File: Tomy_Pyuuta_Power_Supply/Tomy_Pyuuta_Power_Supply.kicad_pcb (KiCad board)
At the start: 2 copper layers, 125 x 45 mm, 15 parts, among them J1 Power In (+12VDC), J2 Power Out, J3 Power LED, U1 +5V Regulator, U2 -5V Regulator

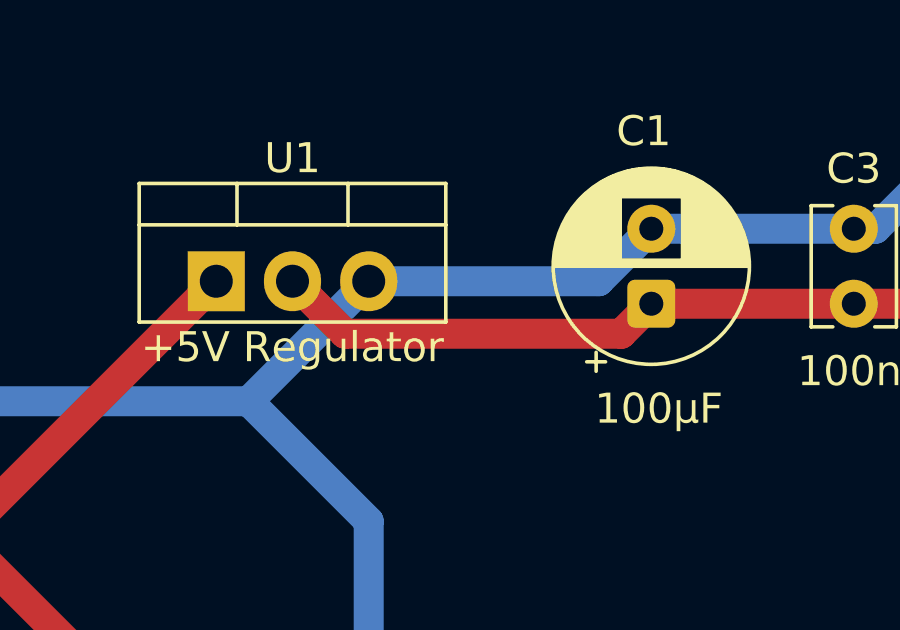
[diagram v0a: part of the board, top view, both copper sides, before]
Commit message: Fixed 5V regulator pinout
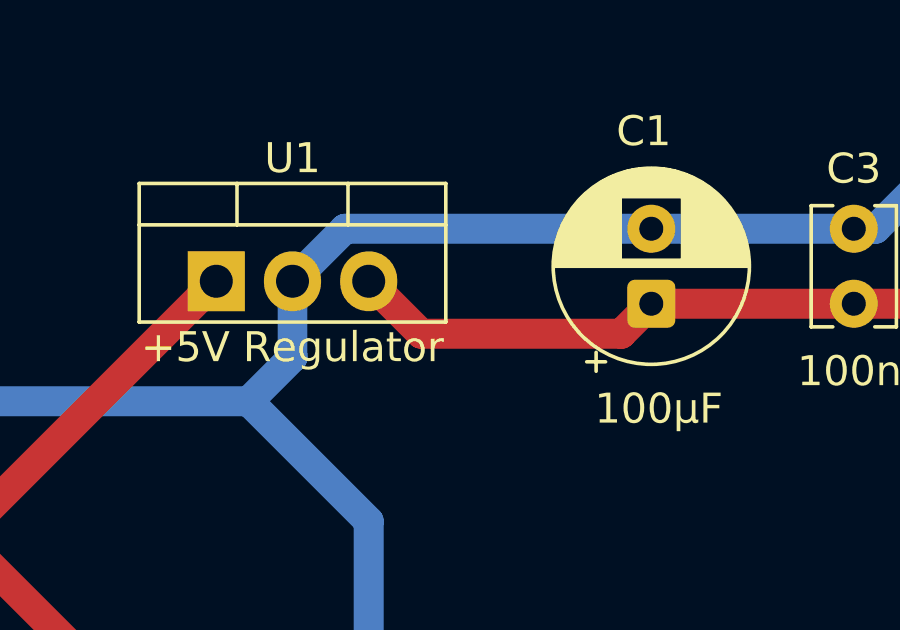
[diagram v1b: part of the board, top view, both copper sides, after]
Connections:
- U1 pad 2: /+5V -> /GND
- U1 pad 3: /GND -> /+5V
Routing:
- net /+5V: track 75.6 -> 73.1 mm
- net /GND: track 143.4 -> 144.9 mm
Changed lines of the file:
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@@
 		(property ki_fp_filters "MountingHole*")
 		(sheetname "/")
-		(sheetfile "Tomy_Pyuta_Power_Supply.kicad_sch")
+		(sheetfile "Tomy_Pyuuta_Power_Supply.kicad_sch")
 		(attr exclude_from_pos_files exclude_from_bom)
 		(fp_circle
@@
 		(property ki_fp_filters "BarrelJack*")
 		(sheetname "/")
-		(sheetfile "Tomy_Pyuta_Power_Supply.kicad_sch")
+		(sheetfile "Tomy_Pyuuta_Power_Supply.kicad_sch")
 		(attr through_hole)
 		(fp_line
@@
 		(property ki_fp_filters "CP_*")
 		(sheetname "/")
-		(sheetfile "Tomy_Pyuta_Power_Supply.kicad_sch")
+		(sheetfile "Tomy_Pyuuta_Power_Supply.kicad_sch")
 		(attr through_hole)
 		(fp_line
@@
 		(property ki_fp_filters "CP_*")
 		(sheetname "/")
-		(sheetfile "Tomy_Pyuta_Power_Supply.kicad_sch")
+		(sheetfile "Tomy_Pyuuta_Power_Supply.kicad_sch")
 		(attr through_hole)
 		(fp_line
@@
 		)
 		(sheetname "/")
-		(sheetfile "Tomy_Pyuta_Power_Supply.kicad_sch")
+		(sheetfile "Tomy_Pyuuta_Power_Supply.kicad_sch")
 		(attr through_hole)
 		(fp_line
@@
 		(property ki_fp_filters "MountingHole*")
 		(sheetname "/")
-		(sheetfile "Tomy_Pyuta_Power_Supply.kicad_sch")
+		(sheetfile "Tomy_Pyuuta_Power_Supply.kicad_sch")
 		(attr exclude_from_pos_files exclude_from_bom)
 		(fp_circle
@@
 		(property ki_fp_filters "MountingHole*")
 		(sheetname "/")
-		(sheetfile "Tomy_Pyuta_Power_Supply.kicad_sch")
+		(sheetfile "Tomy_Pyuuta_Power_Supply.kicad_sch")
 		(attr exclude_from_pos_files exclude_from_bom)
 		(fp_circle
@@
 		)
 		(sheetname "/")
-		(sheetfile "Tomy_Pyuta_Power_Supply.kicad_sch")
+		(sheetfile "Tomy_Pyuuta_Power_Supply.kicad_sch")
 		(attr through_hole)
 		(fp_line
@@
 			(layers "*.Cu" "*.Mask")
 			(remove_unused_layers no)
-			(net 3 "/+5V")
-			(pinfunction "V_{OUT}")
+			(net 2 "/GND")
+			(pinfunction "GND")
 			(pintype "power_out")
 		)
@@
 			(layers "*.Cu" "*.Mask")
 			(remove_unused_layers no)
-			(net 2 "/GND")
-			(pinfunction "GND")
+			(net 3 "/+5V")
+			(pinfunction "V_{OUT}")
 			(pintype "power_out")
 		)
@@
 		(property ki_fp_filters "Connector*:*_1x??_*")
 		(sheetname "/")
-		(sheetfile "Tomy_Pyuta_Power_Supply.kicad_sch")
+		(sheetfile "Tomy_Pyuuta_Power_Supply.kicad_sch")
 		(attr through_hole)
 		(fp_line
@@
 		(property ki_fp_filters "C_*")
 		(sheetname "/")
-		(sheetfile "Tomy_Pyuta_Power_Supply.kicad_sch")
+		(sheetfile "Tomy_Pyuuta_Power_Supply.kicad_sch")
 		(attr through_hole)
 		(fp_line
@@
 		(property ki_fp_filters "*Fuse*")
 		(sheetname "/")
-		(sheetfile "Tomy_Pyuta_Power_Supply.kicad_sch")
+		(sheetfile "Tomy_Pyuuta_Power_Supply.kicad_sch")
 		(attr through_hole)
 		(fp_line
@@
 		(property ki_fp_filters "MountingHole*")
 		(sheetname "/")
-		(sheetfile "Tomy_Pyuta_Power_Supply.kicad_sch")
+		(sheetfile "Tomy_Pyuuta_Power_Supply.kicad_sch")
 		(attr exclude_from_pos_files exclude_from_bom)
 		(fp_circle
@@
 		(property ki_fp_filters "C_*")
 		(sheetname "/")
-		(sheetfile "Tomy_Pyuta_Power_Supply.kicad_sch")
+		(sheetfile "Tomy_Pyuuta_Power_Supply.kicad_sch")
 		(attr through_hole)
 		(fp_line
@@
 		(property ki_fp_filters "Connector*:*_1x??_*")
 		(sheetname "/")
-		(sheetfile "Tomy_Pyuta_Power_Supply.kicad_sch")
+		(sheetfile "Tomy_Pyuuta_Power_Supply.kicad_sch")
 		(attr through_hole)
 		(fp_line
@@
 		(property ki_fp_filters "R_*")
 		(sheetname "/")
-		(sheetfile "Tomy_Pyuta_Power_Supply.kicad_sch")
+		(sheetfile "Tomy_Pyuuta_Power_Supply.kicad_sch")
 		(attr through_hole)
 		(fp_line
@@
 	(segment
 		(start 135.08 94.25)
+		(end 136.54 92.79)
+		(width 1)
+		(layer "B.Cu")
+		(net 2)
+	)
+	(segment
+		(start 135.08 94.25)
 		(end 139.08 98.25)
 		(width 1)
@@
 	)
 	(segment
-		(start 146.75 90.25)
-		(end 148.5 88.5)
+		(start 139.08 110.17)
+		(end 139 110.25)
 		(width 1)
 		(layer "B.Cu")
@@
 	)
 	(segment
-		(start 135.08 94.25)
-		(end 139.08 90.25)
+		(start 148.5 88.5)
+		(end 138.29 88.5)
 		(width 1)
 		(layer "B.Cu")
@@
 	)
 	(segment
-		(start 139.08 110.17)
-		(end 139 110.25)
+		(start 136.54 92.79)
+		(end 136.54 90.25)
 		(width 1)
 		(layer "B.Cu")
@@
 	)
 	(segment
-		(start 155 109)
-		(end 155.25 109.25)
+		(start 138.29 88.5)
+		(end 136.54 90.25)
 		(width 1)
 		(layer "B.Cu")
@@
 	)
 	(segment
-		(start 139.08 90.25)
-		(end 146.75 90.25)
+		(start 155 109)
+		(end 155.25 109.25)
 		(width 1)
 		(layer "B.Cu")
@@
 	)
 	(segment
-		(start 136.54 90.25)
-		(end 138.29 92)
+		(start 140.83 92)
+		(end 147.5 92)
 		(width 1)
 		(layer "F.Cu")
@@
 	)
 	(segment
-		(start 138.29 92)
-		(end 147.5 92)
+		(start 147.5 92)
+		(end 148.5 91)
 		(width 1)
 		(layer "F.Cu")
@@
 	)
 	(segment
-		(start 179.04 114.5)
-		(end 179.04 95.79)
+		(start 139.08 90.25)
+		(end 140.83 92)
 		(width 1)
 		(layer "F.Cu")
@@
 	)
 	(segment
-		(start 180.41 82.25)
-		(end 180.41 84.84)
+		(start 179.04 114.5)
+		(end 179.04 95.79)
 		(width 1)
 		(layer "F.Cu")
@@
 	)
 	(segment
-		(start 147.5 92)
-		(end 148.5 91)
+		(start 180.41 82.25)
+		(end 180.41 84.84)
 		(width 1)
 		(layer "F.Cu")

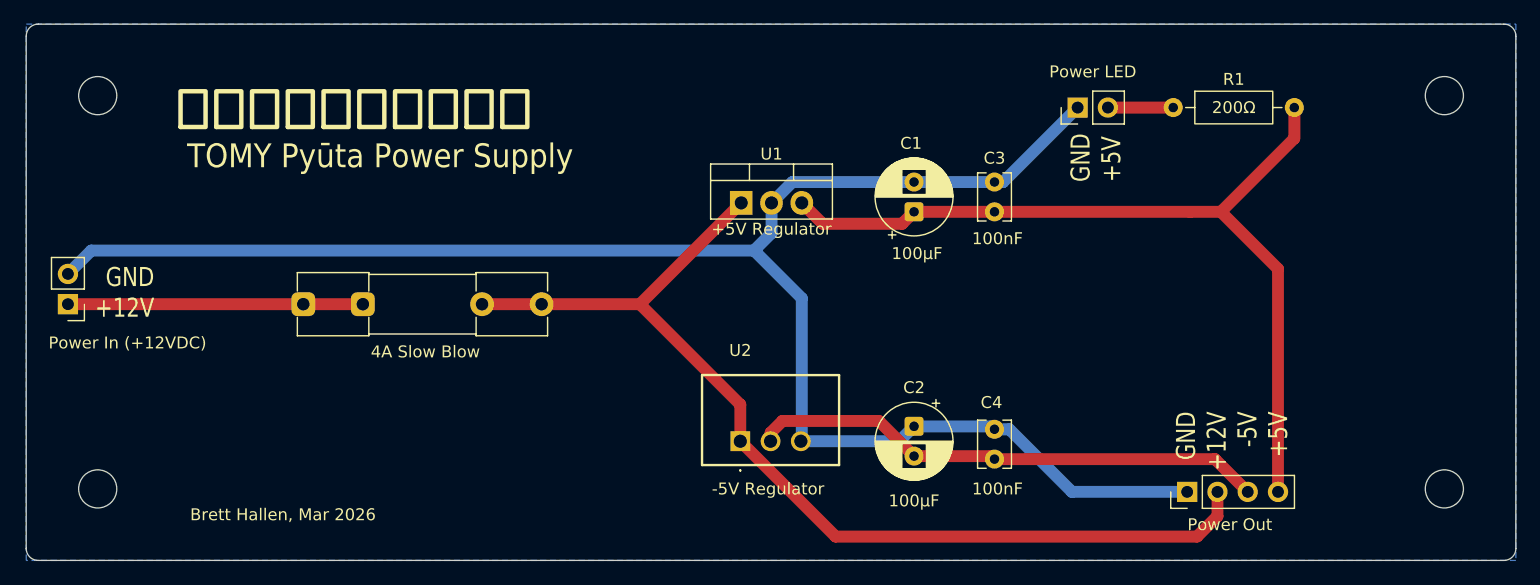
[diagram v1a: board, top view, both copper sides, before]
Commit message: Updated power connecters to JST
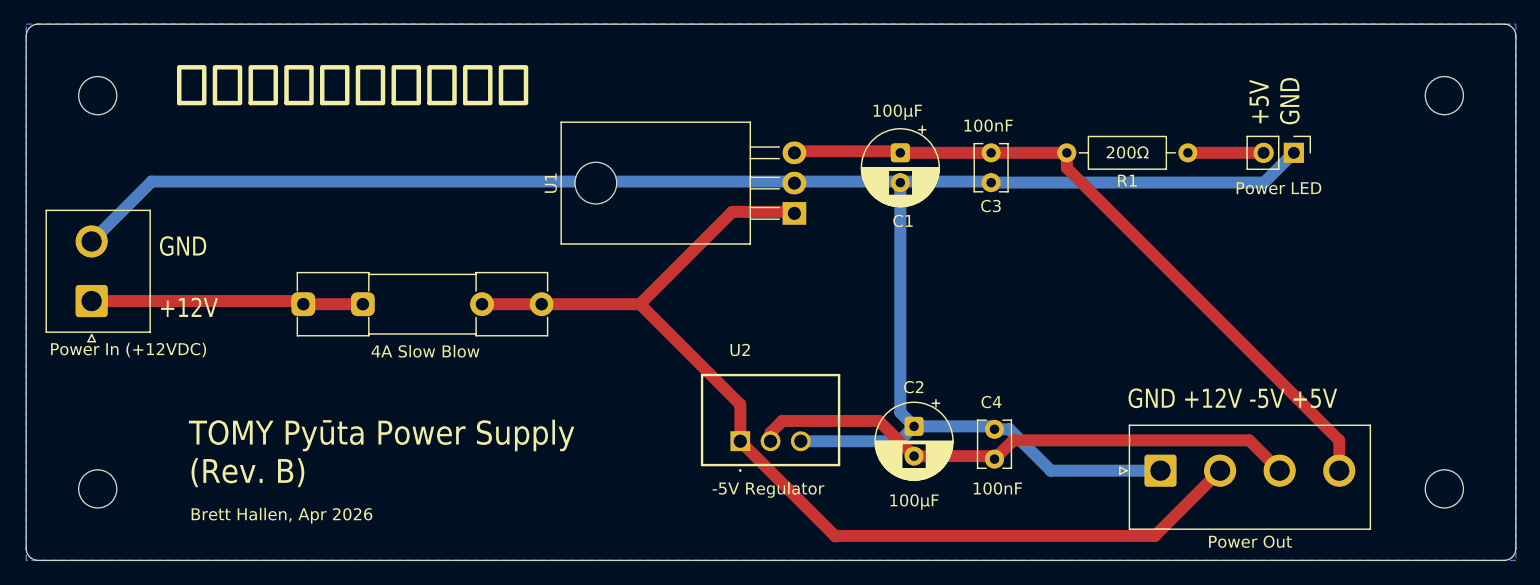
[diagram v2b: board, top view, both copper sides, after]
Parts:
- J1: footprint Connector_PinHeader_2.54mm:PinHeader_1x02_P2.54mm_Vertical -> Connector_JST:JST_NV_B02P-NV_1x02_P5.00mm_Vertical
- J2: footprint Connector_PinHeader_2.54mm:PinHeader_1x04_P2.54mm_Vertical -> Connector_JST:JST_NV_B04P-NV_1x04_P5.00mm_Vertical
- U1: footprint Package_TO_SOT_THT:TO-220-3_Vertical -> Package_TO_SOT_THT:TO-220-3_Horizontal_TabDown
- moved J3 18.5 mm to (180.4, 86.0), turned to -90 degrees
- moved C1 5.08 mm to (147.3, 86.0), turned to -90 degrees
- moved C3 4.96 mm to (155.0, 86.0), turned to -90 degrees
- moved U1 4.55 mm to (138.5, 91.1), turned to 90 degrees
- moved R1 3.99 mm to (171.5, 86.0), turned to 180 degrees
- moved J2 2.86 mm to (169.2, 112.7), turned to 0 degrees
- moved J1 2.01 mm to (79.5, 98.5), turned to 90 degrees
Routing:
- net /+5V: track 73.1 -> 59.1 mm
- net /GND: track 144.9 -> 157.3 mm
- net /+12V: track 86.7 -> 90.6 mm
- net /-5V: track 43.6 -> 46.9 mm
- net /+12V_{IN}: track 24.8 -> 22.9 mm
- net Net-(J3-Pin_2): track 5.49 -> 6.35 mm
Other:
- board text added: "+5V GND"
- board text added: "Brett Hallen, Apr 2026"
- board text added: "TOMY Pyūta Power Supply (Rev. B)"
- board text removed: "Brett Hallen, Mar 2026"
- board text removed: "GND +5V"
- board text removed: "TOMY Pyūta Power Supply"

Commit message: Routing changes
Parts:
- moved C4 4.16 mm to (155.0, 107.6)
- moved C2 3.90 mm to (148.5, 105.1)
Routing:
- net /GND: track 157.3 -> 139.8 mm
- net /-5V: track 46.9 -> 45.9 mm
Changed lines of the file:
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@@
 	(footprint "Capacitor_THT:CP_Radial_D6.3mm_P2.50mm"
 		(layer "F.Cu")
-		(at 148.5 109 -90)
+		(at 148.5 105.1 -90)
 		(descr "CP, Radial series, Radial, pin pitch=2.50mm, diameter=6.3mm, height=7mm, Electrolytic Capacitor")
 		(tags "CP Radial series Radial pin pitch 2.50mm diameter 6.3mm height 7mm Electrolytic Capacitor")
@@
 	(footprint "Capacitor_THT:C_Disc_D3.8mm_W2.6mm_P2.50mm"
 		(layer "F.Cu")
-		(at 155.25 111.75 90)
+		(at 154.97 107.6 90)
 		(descr "C, Disc series, Radial, pin pitch=2.50mm, diameter*width=3.8*2.6mm^2, Capacitor, http://www.vishay.com/docs/45233/krseries.pdf")
 		(tags "C Disc series Radial pin pitch 2.50mm diameter 3.8mm width 2.6mm Capacitor")
@@
 		(tags "TO-220-3 Horizontal RM 2.54mm")
 		(property "Reference" "U1"
-			(at 2.54 -20.41 90)
+			(at 8.89 -6.35 180)
 			(layer "F.SilkS")
 			(effects
@@
 		)
 		(property "Value" "+5V Regulator"
-			(at 2.54 1.95 90)
-			(layer "F.Fab")
+			(at -3.81 -11.43 180)
+			(layer "F.SilkS")
 			(effects
 				(font
@@
 	)
 	(segment
-		(start 141.87 118.2)
-		(end 141.92 118.25)
-		(width 1)
-		(layer "F.Cu")
-		(net 1)
-	)
-	(segment
 		(start 112.25 98.75)
 		(end 125.5 98.75)
@@
 	)
 	(segment
-		(start 159.97 112.72)
-		(end 156.5 109.25)
+		(start 127.2125 93.4875)
+		(end 79.49 93.4875)
 		(width 1)
 		(layer "B.Cu")
@@
 	)
 	(segment
-		(start 147.35 88.55)
-		(end 147.35 107.85)
-		(width 1)
-		(layer "B.Cu")
-		(net 2)
-	)
-	(segment
-		(start 148.5 109)
-		(end 155 109)
-		(width 1)
-		(layer "B.Cu")
-		(net 2)
-	)
-	(segment
-		(start 155.25 109.25)
-		(end 156.5 109.25)
+		(start 154.97 105.1)
+		(end 161.56 105.1)
 		(width 1)
 		(layer "B.Cu")
@@
 	)
 	(segment
-		(start 147.35 107.85)
-		(end 148.5 109)
+		(start 79.6725 93.67)
+		(end 79.49 93.4875)
 		(width 1)
 		(layer "B.Cu")
@@
 	)
 	(segment
-		(start 84.5175 88.46)
-		(end 138.46 88.46)
+		(start 148.5 105.1)
+		(end 154.97 105.1)
 		(width 1)
 		(layer "B.Cu")
@@
 	)
 	(segment
-		(start 79.49 93.4875)
-		(end 84.5175 88.46)
+		(start 138.46 88.46)
+		(end 154.88 88.46)
 		(width 1)
 		(layer "B.Cu")
@@
 	)
 	(segment
-		(start 138.46 88.46)
-		(end 154.88 88.46)
+		(start 154.88 88.46)
+		(end 154.97 88.55)
 		(width 1)
 		(layer "B.Cu")
@@
 	)
 	(segment
-		(start 147.25 110.25)
-		(end 148.5 109)
+		(start 132.11 88.59)
+		(end 127.2125 93.4875)
 		(width 1)
 		(layer "B.Cu")
@@
 	)
 	(segment
-		(start 154.88 88.46)
-		(end 154.97 88.55)
+		(start 161.56 105.1)
+		(end 169.18 112.72)
 		(width 1)
 		(layer "B.Cu")
@@
 	)
 	(segment
-		(start 139 110.25)
-		(end 147.25 110.25)
+		(start 177.87 88.55)
+		(end 180.37 86.05)
 		(width 1)
 		(layer "B.Cu")
@@
 	)
 	(segment
-		(start 177.87 88.55)
-		(end 180.37 86.05)
+		(start 143.35 110.25)
+		(end 148.5 105.1)
 		(width 1)
 		(layer "B.Cu")
@@
 	)
 	(segment
-		(start 155 109)
-		(end 155.25 109.25)
+		(start 138.46 88.59)
+		(end 132.11 88.59)
 		(width 1)
 		(layer "B.Cu")
@@
 	)
 	(segment
-		(start 169.18 112.72)
-		(end 159.97 112.72)
+		(start 139 110.25)
+		(end 143.35 110.25)
 		(width 1)
 		(layer "B.Cu")
@@
 	)
 	(segment
-		(start 155.25 111.75)
-		(end 156.82 110.18)
-		(width 1)
-		(layer "F.Cu")
-		(net 4)
-	)
-	(segment
 		(start 136.46 110.25)
-		(end 136.46 109.54)
+		(end 139.11 107.6)
 		(width 1)
 		(layer "F.Cu")
@@
 	)
 	(segment
-		(start 136.46 109.54)
-		(end 137.451 108.549)
-		(width 1)
-		(layer "F.Cu")
-		(net 4)
-	)
-	(segment
-		(start 156.82 110.18)
-		(end 176.64 110.18)
-		(width 1)
-		(layer "F.Cu")
-		(net 4)
-	)
-	(segment
-		(start 155 111.5)
-		(end 155.25 111.75)
-		(width 1)
-		(layer "F.Cu")
-		(net 4)
-	)
-	(segment
-		(start 148.5 111.5)
-		(end 155 111.5)
+		(start 174.06 107.6)
+		(end 179.18 112.72)
 		(width 1)
 		(layer "F.Cu")
@@
 	)
 	(segment
-		(start 137.451 108.549)
-		(end 145.549 108.549)
+		(start 148.5 107.6)
+		(end 154.97 107.6)
 		(width 1)
 		(layer "F.Cu")
@@
 	)
 	(segment
-		(start 145.549 108.549)
-		(end 148.5 111.5)
+		(start 139.11 107.6)
+		(end 148.5 107.6)
 		(width 1)
 		(layer "F.Cu")
@@
 	)
 	(segment
-		(start 176.64 110.18)
-		(end 179.18 112.72)
+		(start 154.97 107.6)
+		(end 174.06 107.6)
 		(width 1)
 		(layer "F.Cu")
